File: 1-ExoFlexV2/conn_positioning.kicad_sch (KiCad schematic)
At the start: 45 parts, among them J47 3, J48 3, J49 3, J50 2, J51 2, J52 2, J53 4, J54 4, J55 4

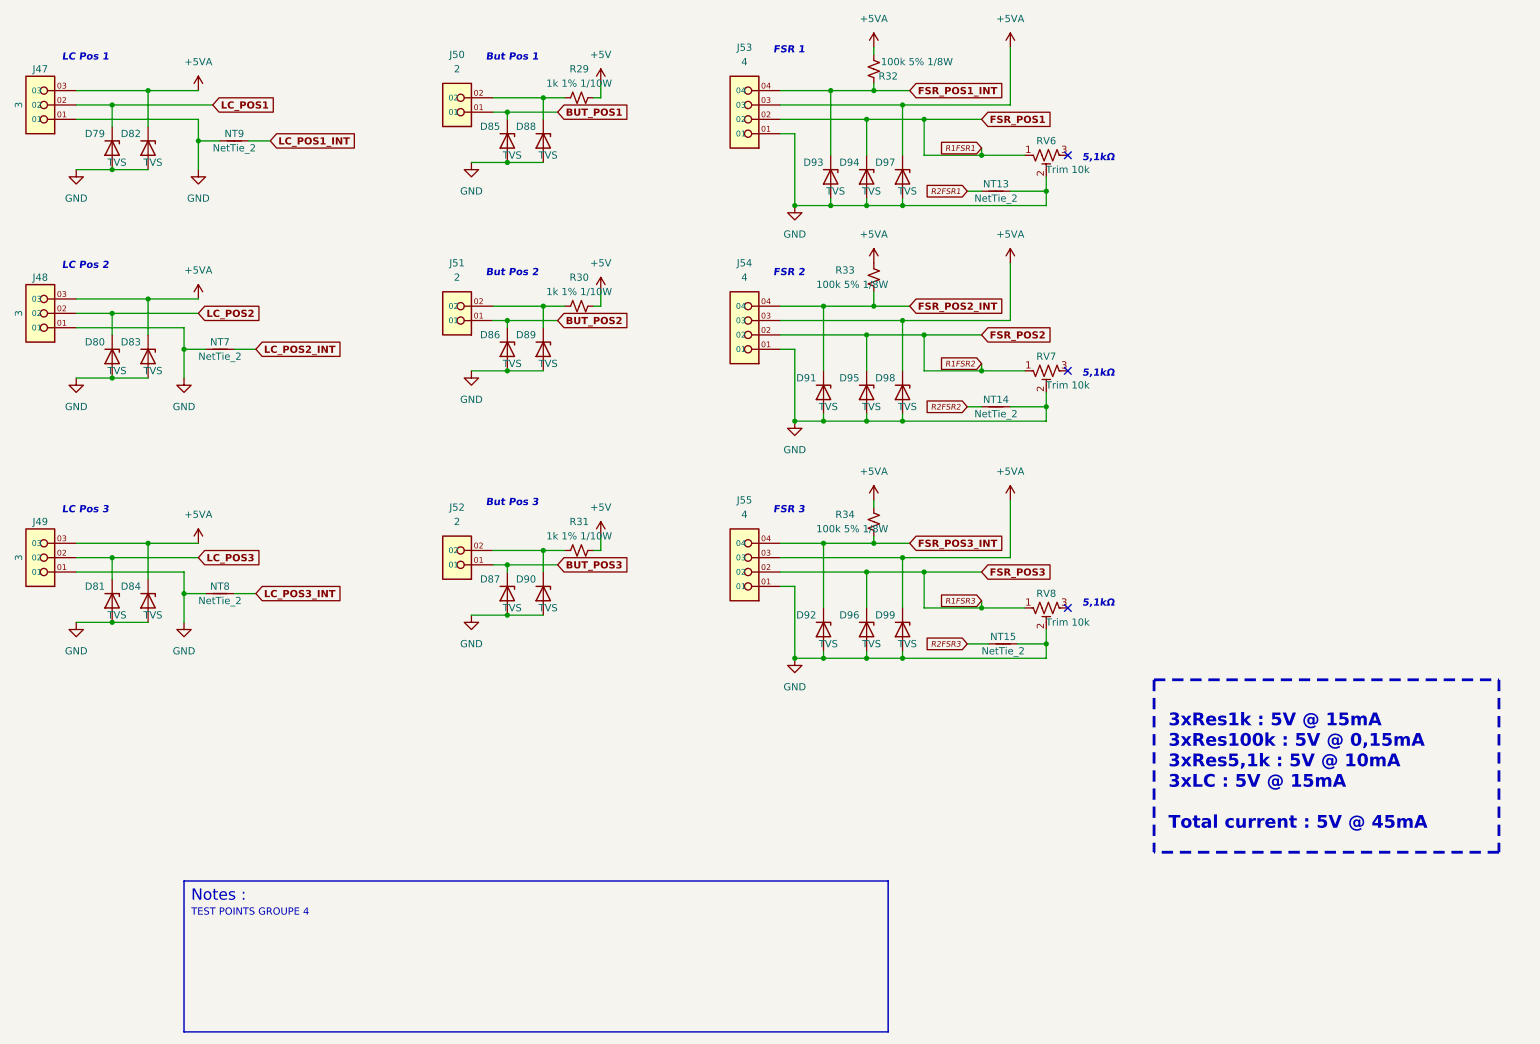
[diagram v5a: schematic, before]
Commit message: Finalisation 3
- Changement des régulateur de tension
- Retrait de test point inutile
- Changement de jumper mal positionner
- Ajout de Mounting holes et fiducial
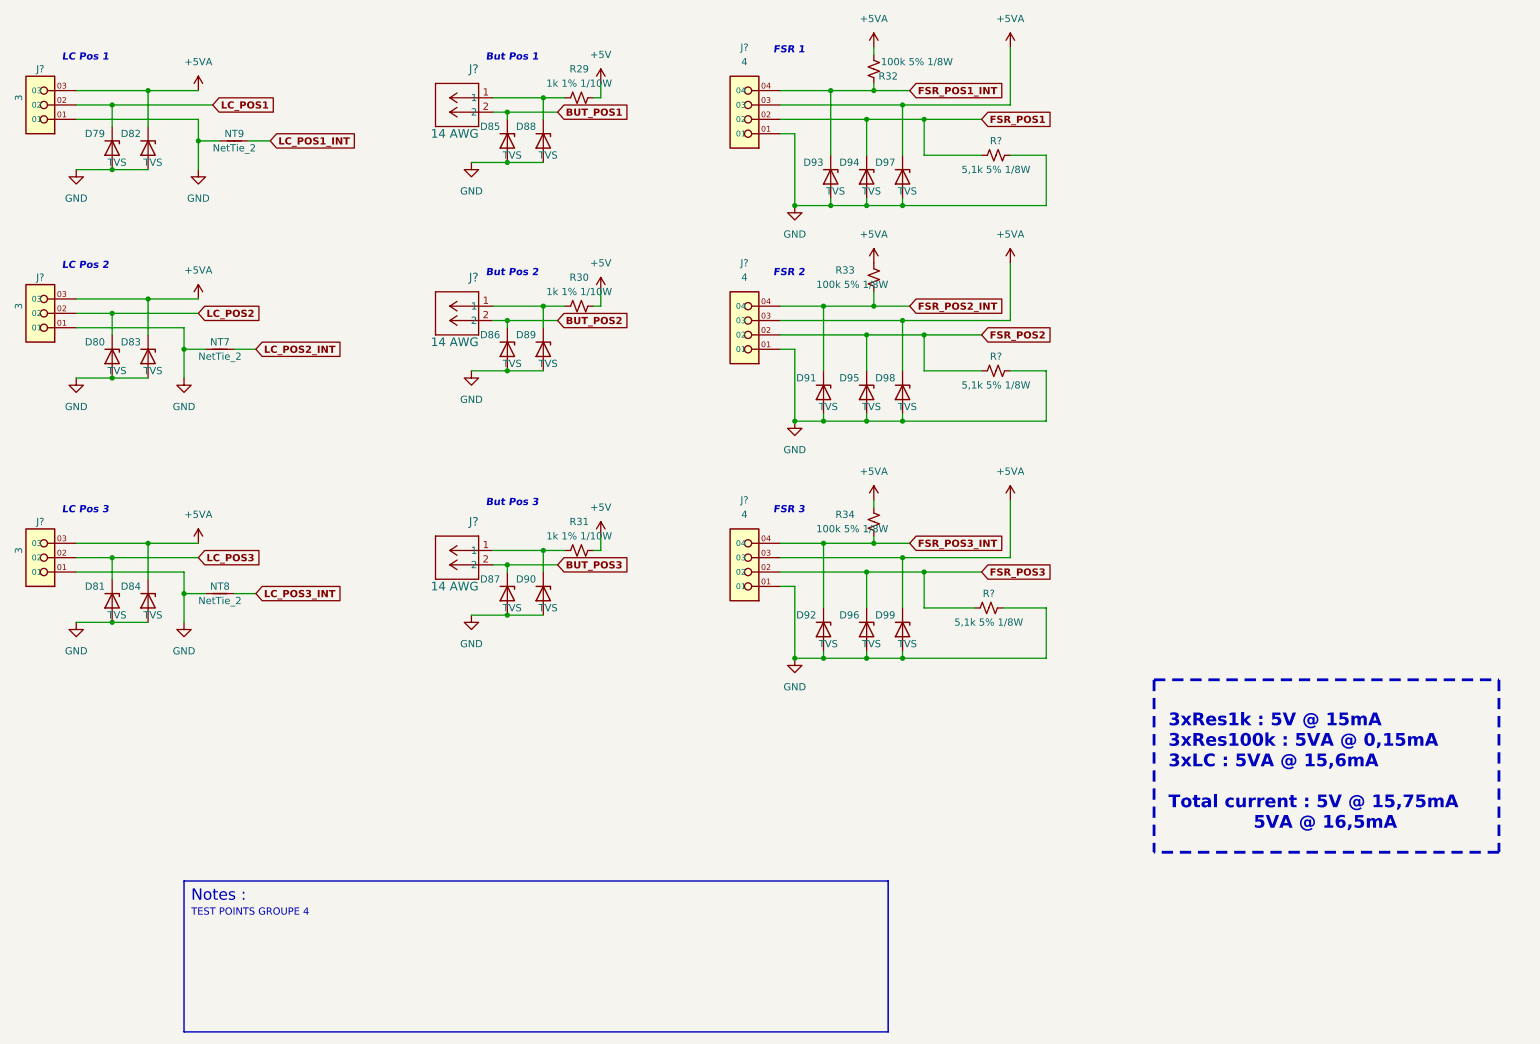
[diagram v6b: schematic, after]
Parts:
- removed J47, J48, J49: 3, FootPrint:PHOENIX_1751109, symbol SymLib:1751109
- removed J50, J51, J52: 2, FootPrint:PHOENIX_1751099, symbol SymLib:1751099
- removed J53, J54, J55: 4, FootPrint:PHOENIX_1751112, symbol SymLib:1751112
- removed NT13, NT14, NT15: NetTie_2, NetTie:NetTie-2_SMD_Pad0.5mm, symbol Device:NetTie_2
- removed RV6, RV7, RV8: Trim 10k, FootPrint:TRIM_3362P-1-103LF, symbol Device:R_Potentiometer_Trim_US
- added J? (x3): 3, FootPrint:PHOENIX_1755749, symbol SymLib:1751109
- added J? (x3): 14 AWG, FootPrintLib:PHOENIX_1755736, symbol SymLib:1729128
- added J? (x3): 4, FootPrint:PHOENIX_1755752, symbol SymLib:1751112
- added R? (x3): 5,1k 5% 1/8W, Resistor_SMD:R_0805_2012Metric, symbol Device:R_Small_US
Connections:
- net +5VA: now also J?.03, J?.03, J?.03, J?.03, J?.03, J?.03
- net BUT_POS1: now also J?.2
- net BUT_POS2: now also J?.2
- net BUT_POS3: now also J?.2
- net FSR_POS1: now also J?.02, R?.1
- net FSR_POS1_INT: now also J?.04
- net FSR_POS2: now also J?.02, R?.1
- net FSR_POS2_INT: now also J?.04
- net FSR_POS3: now also J?.02, R?.1
- net FSR_POS3_INT: now also J?.04
- net GND: now also J?.01, J?.01, J?.01, J?.01, J?.01, J?.01, R?.2, R?.2, R?.2
- net LC_POS1: now also J?.02
- net LC_POS2: now also J?.02
- net LC_POS3: now also J?.02
- net at D90.1 (K), R31.1: now also J?.1
- net at D88.1 (K), R29.1: now also J?.1
- net at D89.1 (K), R30.1: now also J?.1
- no-connect marks 3 -> 0
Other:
- note added: "3xRes1k : 5V @ 15mA 3xRes100k : 5VA @ 0,15mA 3xLC : 5VA @ 15,6mA Total current : 5V @ 15,75mA 5VA @ 16,5mA"
- note removed: "3xRes1k : 5V @ 15mA 3xRes100k : 5V @ 0,15mA 3xRes5,1k : 5V @ 10mA 3xLC : 5V @ 15mA Total current : 5V @ 45mA"
- note removed: "5,1kΩ"

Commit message: Finalisation schéma FIN
- Changement des uméro pour les inverseurs
- Changement des connecteur et début de placement
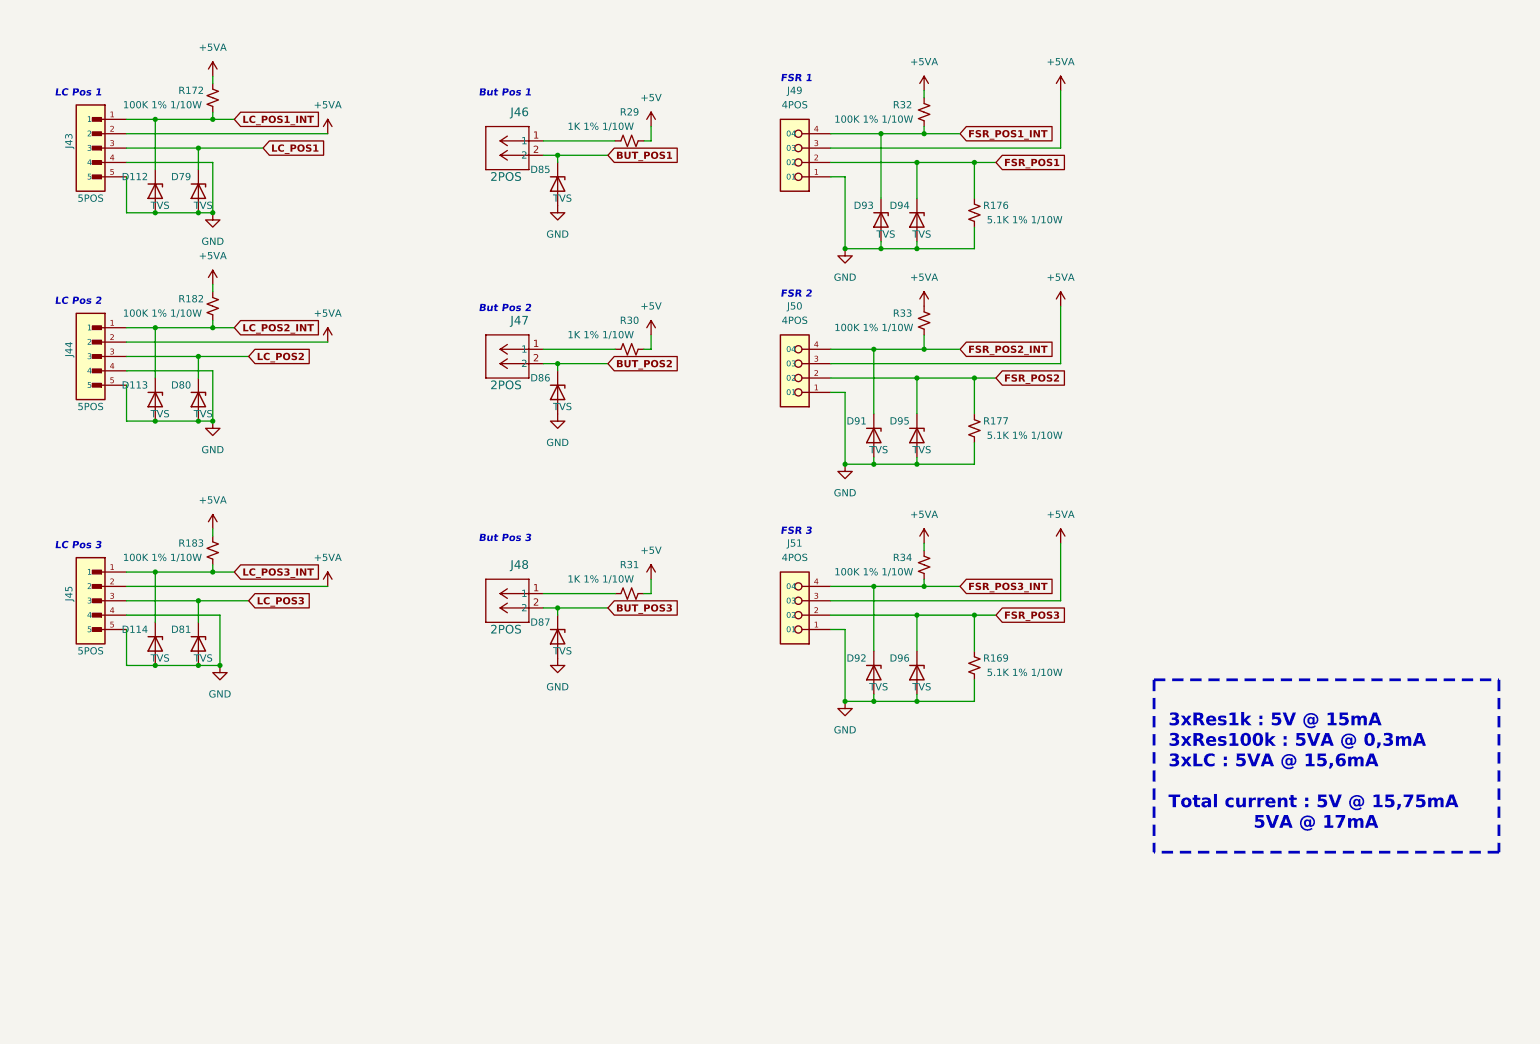
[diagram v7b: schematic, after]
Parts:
- removed D82, D83, D84, D88, D89, D90, D97, D98, D99: TVS, FootPrint:DPY2_TEX, symbol Device:D_Zener
- removed J? (x3): 3, FootPrint:PHOENIX_1755749, symbol SymLib:1751109
- removed J? (x3): 14 AWG, FootPrintLib:PHOENIX_1755736, symbol SymLib:1729128
- removed NT7, NT8, NT9: NetTie_2, NetTie:NetTie-2_SMD_Pad0.5mm, symbol Device:NetTie_2
- added D112, D113, D114: TVS, FootPrint:DPY2_TEX, symbol Device:D_Zener
- added J43, J44, J45: 5POS, FootPrint:CON_39302050, symbol SymLib:1755765
- added J46, J47, J48: 2POS, FootPrintLib:CON_39281023, symbol SymLib:1729128
- added R172, R182, R183: 100K 1% 1/10W, Resistor_SMD:R_0603_1608Metric, symbol Device:R_Small_US
- J49, J50, J51: renamed from J?; value 4 -> 4POS; footprint FootPrint:PHOENIX_1755752 -> FootPrint:CON_39301049; DESCRIPTION 4 Position Terminal Block Header, Male Pins, Shrouded (4 Si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 -> Connector Header Through Hole 4 position 0.165" (4.20mm); MANUFACTURER Phoenix Contact -> Molex; PACKAGE 4 POS 0.200" (5.08mm) -> 4 POS 0.165" (4,2mm); PART NUMBER 1755752 -> 0039301049
- R169, R176, R177: renamed from R?; value 5,1k 5% 1/8W -> 5.1K 1% 1/10W; footprint Resistor_SMD:R_0805_2012Metric -> Resistor_SMD:R_0603_1608Metric; DESCRIPTION 5.1 kOhms ±5% 0.125W, 1/8W Chip Resistor 0805 (2012 Metric)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 -> 5.1 kOhms ±1% 0.1W, 1/10W Chip Resistor 0603 (1608 Metric) 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; PACKAGE 0805 (2012 Metric) -> 0603 (1608 Metric); PART NUMBER ERJ-6GEYJ512V -> ERJ-3EKF5101V
- R29, R30, R31: value 1k 1% 1/10W -> 1K 1% 1/10W; footprint Resistor_SMD:R_0402_1005Metric -> Resistor_SMD:R_0603_1608Metric; DESCRIPTION 1 kOhms ±1% 0.1W, 1/10W Chip Resistor 0402 (1005 Metric) Au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 -> 1 kOhms ±1% 0.1W, 1/10W Chip Resistor 0603 (1608 Metric) Au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; PACKAGE 0402 (1005 Metric) -> 0603 (1608 Metric); PART NUMBER ERJ-2RKF1001X -> ERJ-3EKF1001V
- R32, R33, R34: value 100k 5% 1/8W -> 100K 1% 1/10W; footprint Resistor_SMD:R_0805_2012Metric -> Resistor_SMD:R_0603_1608Metric; DESCRIPTION 100 kOhms ±5% 0.125W, 1/8W Chip Resistor 0805 (2012 Metric)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 -> 100 kOhms ±1% 0.1W, 1/10W Chip Resistor 0603 (1608 Metric) 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; PACKAGE 0805 (2012 Metric) -> 0603 (1608 Metric); PART NUMBER ERJ-6GEYJ104V -> ERJ-3EKF1003V
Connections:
- net +5VA: now also J49.3 (03), J50.3 (03), J51.3 (03), J43.2, J44.2, J45.2, R172.1, R182.1, R183.1; no longer J49.03, J50.03, J51.03
- net BUT_POS1: now also J46.2
- net BUT_POS2: now also J47.2
- net BUT_POS3: now also J48.2
- net FSR_POS1: now also J49.2 (02), R176.2; no longer J49.02, R176.1
- net FSR_POS1_INT: now also J49.4 (04); no longer J49.04
- net FSR_POS2: now also J50.2 (02), R177.2; no longer J50.02, R177.1
- net FSR_POS2_INT: now also J50.4 (04); no longer J50.04
- net FSR_POS3: now also J51.2 (02), R169.2; no longer J51.02, R169.1
- net FSR_POS3_INT: now also J51.4 (04); no longer J51.04
- net GND: now also J49.1 (01), J50.1 (01), J51.1 (01), R169.1, R176.1, R177.1, D112.2 (A), D113.2 (A), D114.2 (A), J43.4, J43.5, J44.4, J44.5, J45.4, J45.5; no longer J49.01, J50.01, J51.01, R169.2, R176.2, R177.2
- net LC_POS1: now also J43.3
- net LC_POS1_INT: now also D112.1 (K), J43.1, R172.2
- net LC_POS2: now also J44.3
- net LC_POS2_INT: now also D113.1 (K), J44.1, R182.2
- net LC_POS3: now also J45.3
- net LC_POS3_INT: now also D114.1 (K), J45.1, R183.2
- net at R31.1: now also J48.1
- net at R29.1: now also J46.1
- net at R30.1: now also J47.1
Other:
- note added: "3xRes1k : 5V @ 15mA 3xRes100k : 5VA @ 0,3mA 3xLC : 5VA @ 15,6mA Total current : 5V @ 15,75mA 5VA @ 17mA"
- note removed: "3xRes1k : 5V @ 15mA 3xRes100k : 5VA @ 0,15mA 3xLC : 5VA @ 15,6mA Total current : 5V @ 15,75mA 5VA @ 16,5mA"
- note removed: "Notes :"
- note removed: "TEST POINTS GROUPE 4"
- moved on the sheet: D79, D80, D81, D85, D86, D87, D91, D92, D93, D94, D95, D96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
